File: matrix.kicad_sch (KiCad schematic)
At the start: 164 parts, among them SW1 SW_Push_45deg, SW10 SW_Push_45deg, SW11 SW_Push_45deg, SW12 SW_Push_45deg, SW13 SW_Push_45deg, SW14 SW_Push_45deg, SW15 SW_Push_45deg, SW16 SW_Push_45deg, SW17 SW_Push_45deg, SW18 SW_Push_45deg, SW19 SW_Push_45deg, SW2 SW_Push_45deg, SW20 SW_Push_45deg, SW21 SW_Push_45deg, SW22 SW_Push_45deg, SW23 SW_Push_45deg, SW24 SW_Push_45deg, SW25 SW_Push_45deg, SW26 SW_Push_45deg, SW27 SW_Push_45deg, SW28 SW_Push_45deg, SW29 SW_Push_45deg, SW3 SW_Push_45deg, SW30 SW_Push_45deg, SW31 SW_Push_45deg, SW32 SW_Push_45deg, SW33 SW_Push_45deg, SW34 SW_Push_45deg, SW35 SW_Push_45deg, SW36 SW_Push_45deg, SW37 SW_Push_45deg, SW38 SW_Push_45deg, SW39 SW_Push_45deg, SW4 SW_Push_45deg, SW40 SW_Push_45deg, SW41 SW_Push_45deg, SW42 SW_Push_45deg, SW43 SW_Push_45deg, SW44 SW_Push_45deg, SW45 SW_Push_45deg, SW46 SW_Push_45deg, SW47 SW_Push_45deg, SW48 SW_Push_45deg, SW49 SW_Push_45deg, SW5 SW_Push_45deg, SW50 SW_Push_45deg, SW51 SW_Push_45deg, SW52 SW_Push_45deg, SW53 SW_Push_45deg, SW54 SW_Push_45deg, SW55 SW_Push_45deg, SW56 SW_Push_45deg, SW57 SW_Push_45deg, SW58 SW_Push_45deg, SW59 SW_Push_45deg, SW6 SW_Push_45deg, SW60 SW_Push_45deg, SW61 SW_Push_45deg, SW62 SW_Push_45deg, SW63 SW_Push_45deg, SW64 SW_Push_45deg, SW65 SW_Push_45deg, SW66 SW_Push_45deg, SW67 SW_Push_45deg, SW68 SW_Push_45deg, SW69 SW_Push_45deg, SW7 SW_Push_45deg, SW70 SW_Push_45deg, SW71 SW_Push_45deg, SW72 SW_Push_45deg, SW73 SW_Push_45deg, SW74 SW_Push_45deg, SW75 SW_Push_45deg, SW76 SW_Push_45deg, SW77 SW_Push_45deg, SW78 SW_Push_45deg, SW79 SW_Push_45deg, SW8 SW_Push_45deg, SW80 SW_Push_45deg, SW81 SW_Push_45deg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

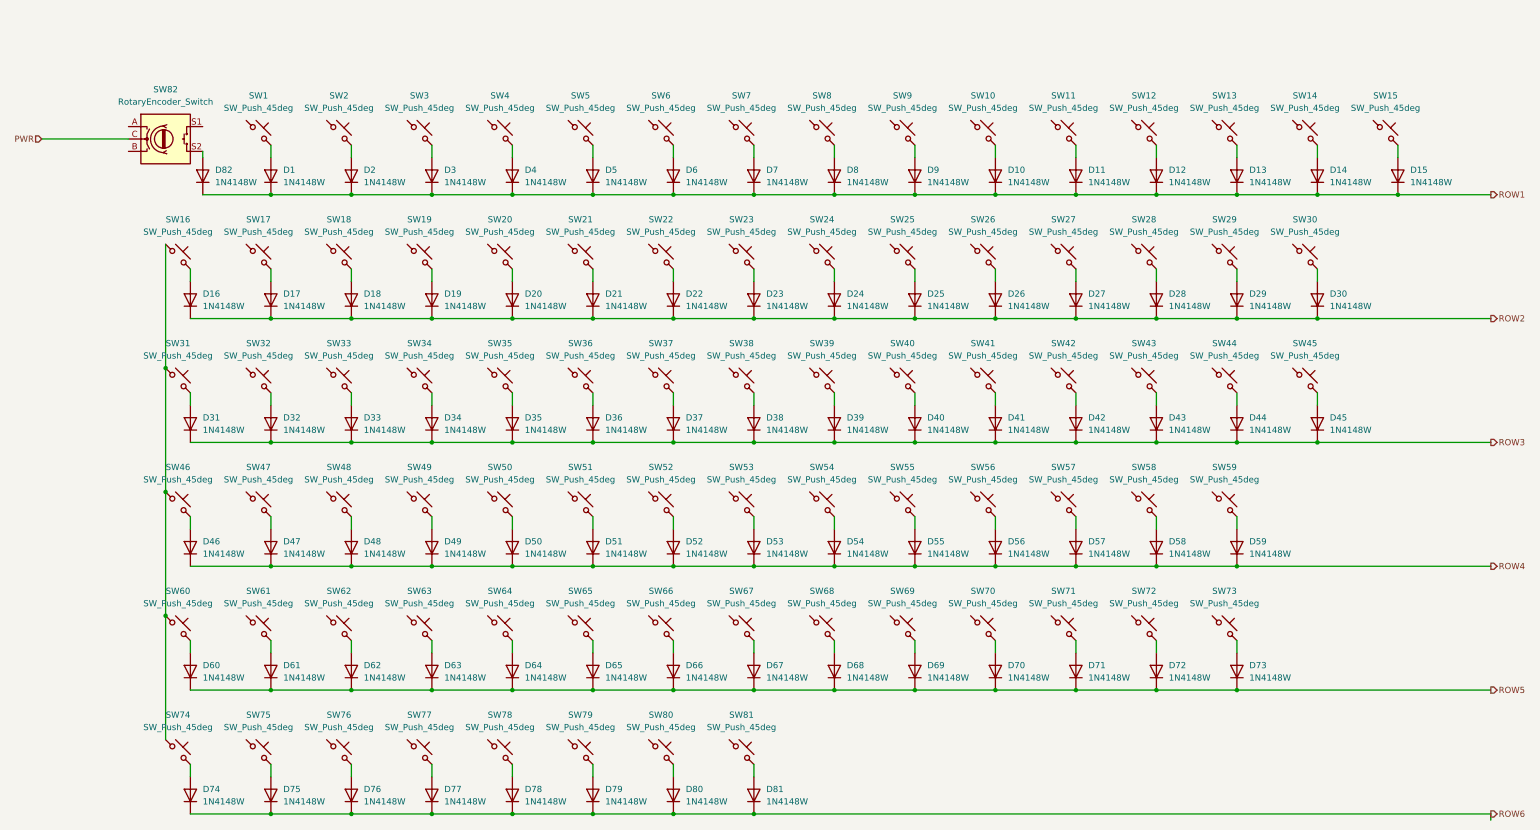
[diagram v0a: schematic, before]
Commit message: added oscillator and memory
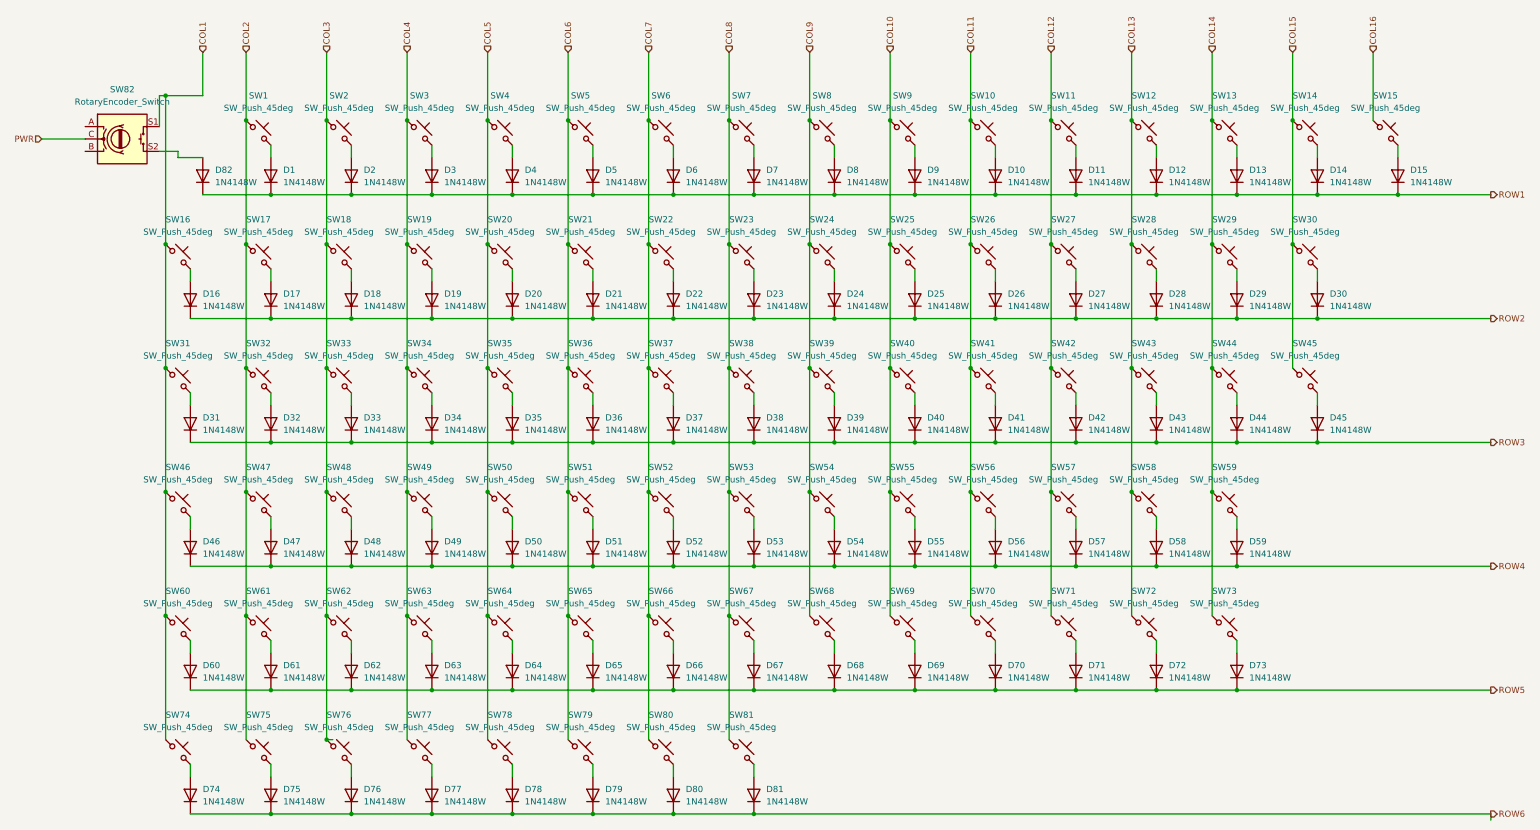
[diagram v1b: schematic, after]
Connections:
- net COL2: now reaches SW61.1
- net COL2: now also SW1.1, SW17.1, SW32.1, SW47.1, SW75.1
- net COL4: now reaches SW3.1
- net COL4: now also SW19.1, SW34.1, SW49.1, SW63.1, SW77.1
- net COL5: now reaches SW78.1
- net COL5: now also SW20.1, SW35.1, SW4.1, SW50.1, SW64.1
- net COL8: now reaches SW53.1
- net COL8: now also SW23.1, SW38.1, SW67.1, SW7.1, SW81.1
- net COL12: now reaches SW71.1
- net COL12: now also SW11.1, SW27.1, SW42.1, SW57.1
- net COL10: now reaches SW55.1
- net COL10: now also SW25.1, SW40.1, SW69.1, SW9.1
- net COL3: now reaches SW33.1
- net COL3: now also SW18.1, SW2.1, SW48.1, SW62.1, SW76.1
- net COL11: now reaches SW10.1
- net COL11: now also SW26.1, SW41.1, SW56.1, SW70.1
- net COL7: now reaches SW52.1
- net COL7: now also SW22.1, SW37.1, SW6.1, SW66.1, SW80.1
- net COL6: now reaches SW5.1
- net COL6: now also SW21.1, SW36.1, SW51.1, SW65.1, SW79.1
- net COL1: now reaches SW16.1, SW31.1, SW46.1, SW60.1, SW74.1
- net COL1: now also SW82.S1
- net COL9: now reaches SW68.1
- net COL9: now also SW24.1, SW39.1, SW54.1, SW8.1
- net COL13: now reaches SW72.1
- net COL13: now also SW12.1, SW28.1, SW43.1, SW58.1
- net COL14: now reaches SW29.1
- net COL14: now also SW13.1, SW44.1, SW59.1, SW73.1
- net COL15: now reaches SW30.1
- net COL15: now also SW14.1, SW45.1
- net COL16: now reaches SW15.1
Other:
- moved on the sheet: SW82
